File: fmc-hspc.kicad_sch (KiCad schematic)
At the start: 36 parts, among them J18 ASP-184329-01_mounting_holes_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

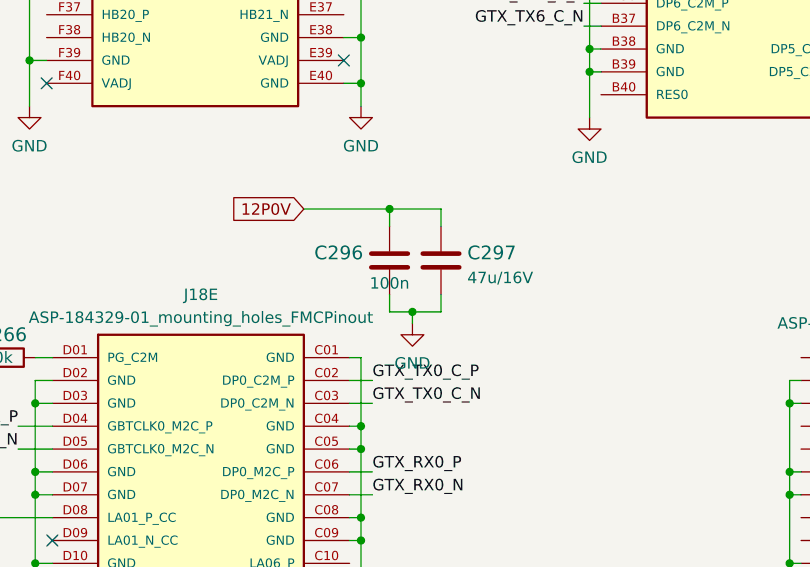
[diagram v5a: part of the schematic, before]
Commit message: Fix 100n value position
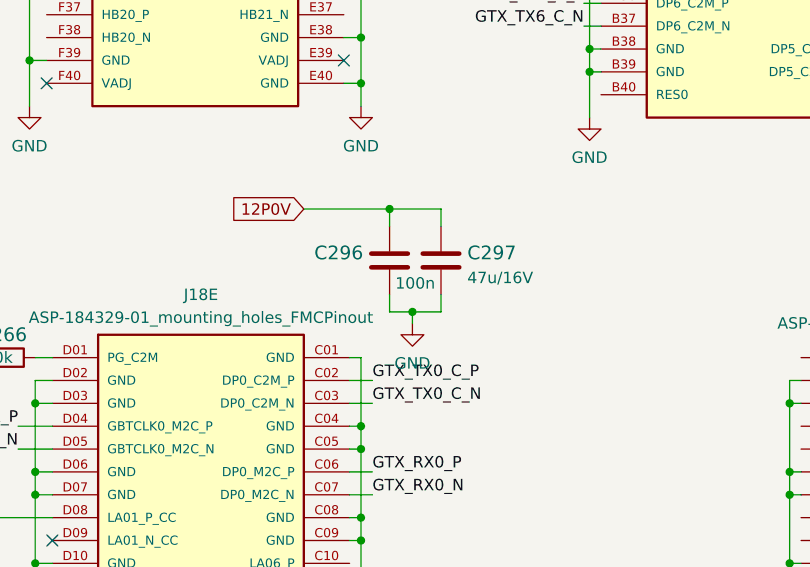
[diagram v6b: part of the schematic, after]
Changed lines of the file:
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@@
       (effects (font (size 1.524 1.524)) (justify left) hide)
     )
-    (property "Val" "100n" (id 6) (at 217.17 153.035 0))
+    (property "Val" "100n" (id 6) (at 217.805 153.035 0)
+      (effects (font (size 1.27 1.27)) (justify left))
+    )
     (pin "1")
     (pin "2")
